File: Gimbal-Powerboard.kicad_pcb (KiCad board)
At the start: 2 copper layers, 165 parts, among them Q1 Q_PMOS_GDS, Q2 Q_PMOS_GDS, Q3 SI4116DY, Q4 SI4116DY, Q5 SI4116DY, Q6 SI4116DY, Q7 SI4116DY, Q8 SI4116DY, U1 DRV8301, U2 NUP4201MR6, U27 2P2T_Switch, U3 LAUNCHXL-F28069M_Launchpad_J1, U4 ACS711, U5 Molex_SL-3, U6 Molex_SL-5, U7 ACS711, U8 MAX_3232

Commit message: Created traces for MAX3232, part of DRV8301
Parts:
- added REF**: Via_P1.27mm_5x5, MRDT_Drill_Holes:Via_.6mm, F.Cu at (141.2, 96.6)
- C10, C11, C12, C13, C14, C15, C16, C17, C18, C20, C21, C23, C24, C25, C26, C27, C3, C32, C33, C34, C35, C4, C6, C7, C8, C9: footprint Capacitors_SMD:C_0805_HandSoldering -> Capacitors_SMD:C_0603_HandSoldering
- C36, C41, C42, C43: footprint Capacitors_SMD:C_0805_HandSoldering -> Capacitors_SMD:C_0603_HandSoldering; moved to B.Cu
- R1, R10, R11, R12, R13, R14, R15, R16, R17, R18, R19, R2, R20, R21, R22, R23, R24, R25, R26, R27, R28, R29, R3, R30, R31, R32, R33, R34, R35, R36, R37, R4, R5, R6, R7, R8, R9: footprint Resistors_SMD:R_0805_HandSoldering -> Capacitors_SMD:C_0603_HandSoldering
- U8: moved to B.Cu
- moved D16 350.5 mm to (317.6, 132.5)
- moved C32 349.8 mm to (357.3, 148.0)
- moved D12 348.0 mm to (318.6, 147.7)
- moved D14 345.1 mm to (335.4, 105.0)
- moved TP6 339.8 mm to (341.4, 138.4)
- moved R27 332.3 mm to (337.4, 144.3)
- moved D15 332.1 mm to (332.6, 75.6)
- moved R29 322.4 mm to (349.6, 151.0)
- moved TP9 314.7 mm to (346.1, 127.6)
- moved C7 313.4 mm to (342.3, 92.3)
- moved R33 310.1 mm to (347.9, 98.3)
- moved TP11 307.6 mm to (347.3, 84.6)
- moved TP3 304.3 mm to (332.6, 136.9)
- moved C11 301.7 mm to (348.7, 91.8)
- moved TP10 299.7 mm to (341.8, 41.4)
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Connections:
- net PVDD renamed 12VACT
- net PVDDSENSE renamed 12VACTSENSE
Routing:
- net VCC: track 0.00 -> 110.1 mm, vias 0 -> 3
- net UART_RX: track 0.00 -> 82.9 mm, vias 0 -> 2
- net UART_TX: track 0.00 -> 79.9 mm, vias 0 -> 2
- net PWM_IN: track 0.00 -> 67.1 mm
- net INL_C/PWM_IN_1: track 0.00 -> 57.5 mm, vias 0 -> 4
- net INL_C/PWM_IN_2: track 0.00 -> 53.2 mm, vias 0 -> 2
- net INL_C: track 0.00 -> 41.3 mm, vias 0 -> 1
- net NSCS: track 0.00 -> 34.0 mm, vias 0 -> 1
- net INH_A: track 0.00 -> 33.9 mm, vias 0 -> 1
- net SCLK: track 0.00 -> 33.3 mm, vias 0 -> 1
- net INL_A: track 0.00 -> 32.7 mm, vias 0 -> 1
- net INH_B: track 0.00 -> 31.4 mm, vias 0 -> 1
- net SDO: track 0.00 -> 31.4 mm, vias 0 -> 1
- net INL_B: track 0.00 -> 30.1 mm, vias 0 -> 1
- net SDI: track 0.00 -> 29.4 mm, vias 0 -> 1
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- added copper zone on B.Cu, net 12VACT
- added copper zone on F.Cu, net PVDD

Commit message: Finished component placement for DRV8301, phase C
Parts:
- C35: moved to B.Cu
- moved C32 250.8 mm to (116.2, 78.6)
- moved C11 248.8 mm to (101.3, 65.4)
- moved D11 248.8 mm to (76.3, 55.9)
- moved D15 248.8 mm to (85.2, 49.1)
- moved D8 248.8 mm to (96.8, 82.0)
- moved R22 248.8 mm to (80.1, 75.3)
- moved R33 248.8 mm to (100.5, 71.9)
- moved R36 248.8 mm to (91.4, 59.2)
- moved TP11 248.8 mm to (99.9, 58.2)
- moved TP5 248.8 mm to (78.5, 65.2)
- moved TP8 248.8 mm to (92.3, 51.8)
- moved C34 248.8 mm to (107.1, 60.7)
- moved C7 248.8 mm to (94.9, 65.9)
- moved D14 248.8 mm to (88.0, 78.6)
- moved R13 248.8 mm to (85.1, 61.1)
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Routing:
- net INL_C/PWM_IN_1: track 57.5 -> 0.00 mm, vias 4 -> 0
- net INL_C/PWM_IN_2: track 53.2 -> 0.79 mm, vias 2 -> 0
- net VCC: track 110.1 -> 63.9 mm, vias 3 -> 1
- net INL_C: track 41.3 -> 0.00 mm, vias 1 -> 0
- net PWM_IN: track 67.1 -> 31.0 mm
- net Net-(D16-Pad2): track 0.00 -> 24.6 mm, vias 0 -> 1
- net NSCS: track 34.0 -> 9.39 mm, vias 1 -> 0
- net DC_CAL: track 16.3 -> 38.6 mm, vias 0 -> 1
- net GND: track 9.56 -> 26.9 mm, vias 0 -> 1
- net Net-(R17-Pad1): track 11.3 -> 12.5 mm

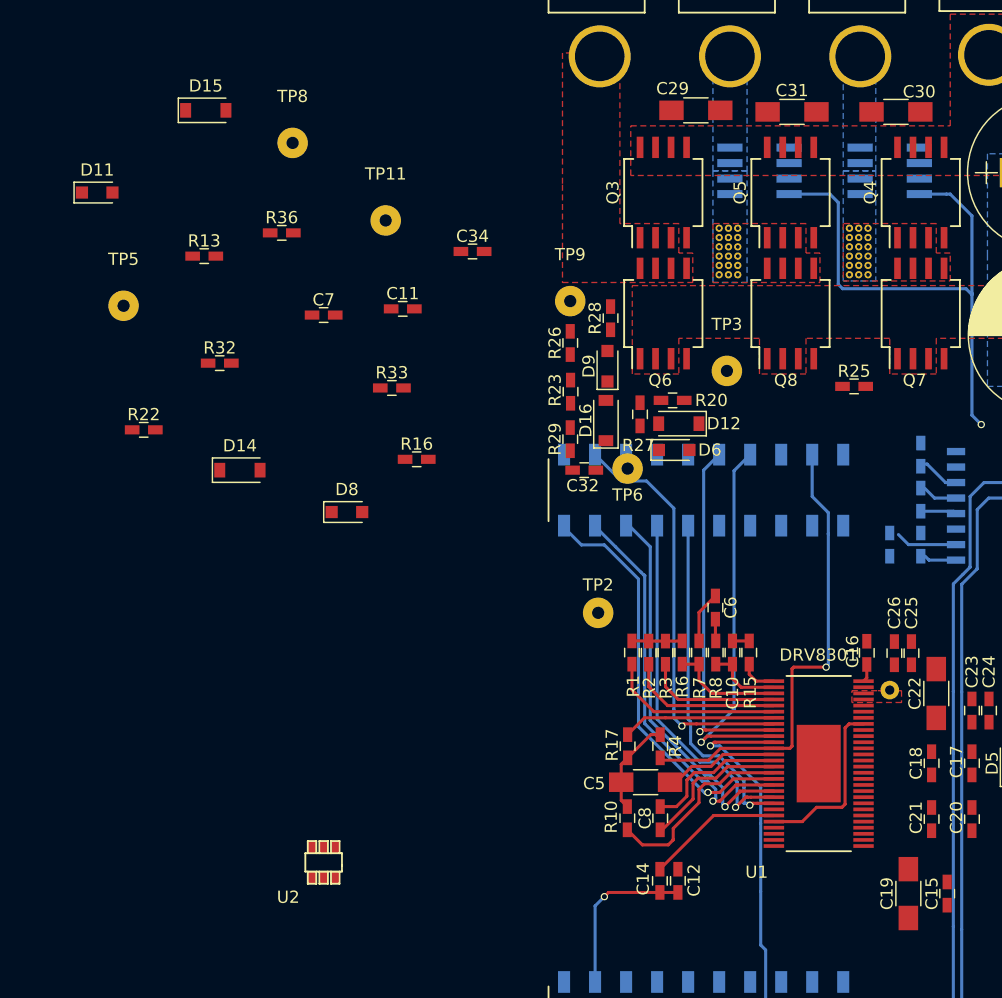
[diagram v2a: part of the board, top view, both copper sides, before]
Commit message: Added components for phase B circuitry
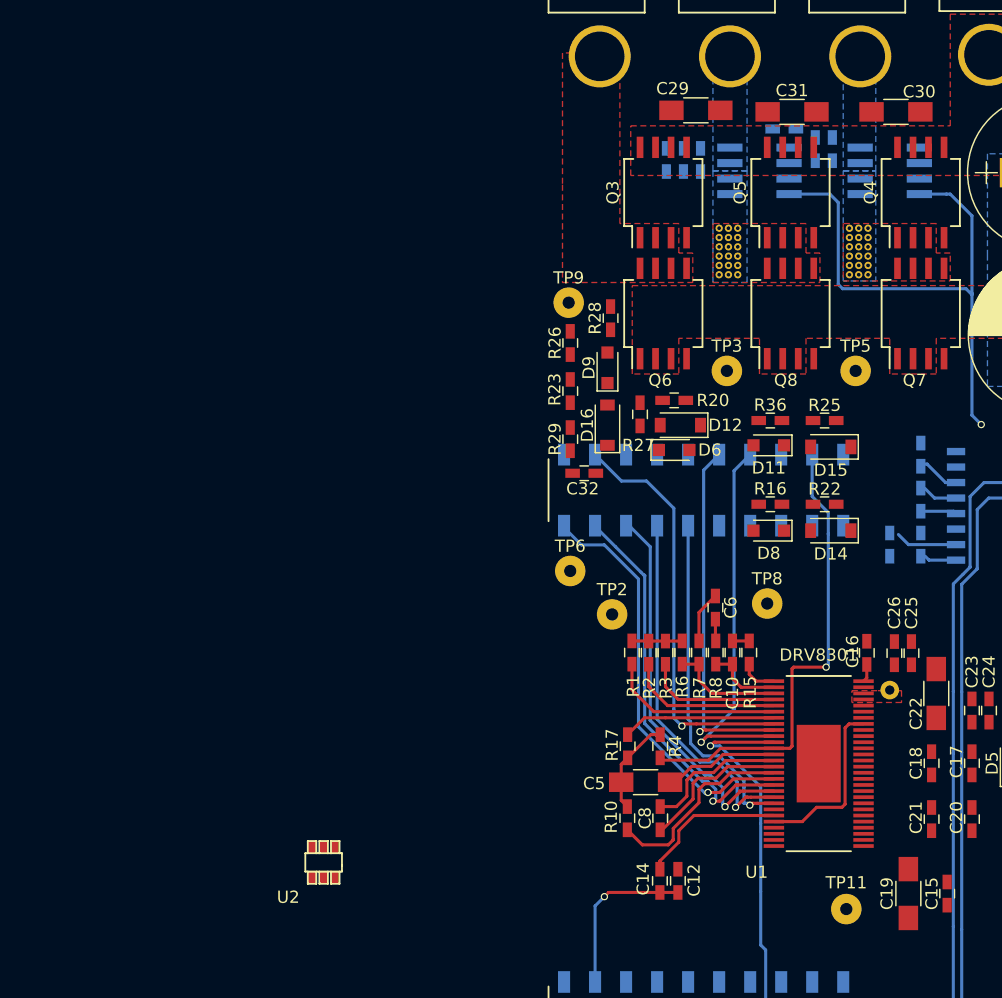
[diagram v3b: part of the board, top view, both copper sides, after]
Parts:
- C11, C34, C7, R13, R32, R33: moved to B.Cu
- moved TP11 67.8 mm to (137.7, 114.6)
- moved TP5 60.2 mm to (138.4, 70.5)
- moved D11 58.8 mm to (131.3, 76.6), turned to 180 degrees
- moved D15 58.1 mm to (136.4, 76.7), turned to 180 degrees
- moved R22 56.1 mm to (135.9, 81.4)
- moved TP8 54.2 mm to (131.2, 89.5)
- moved R13 50.8 mm to (135.1, 52.3), turned to 270 degrees
- moved D14 48.6 mm to (136.4, 83.6), turned to 180 degrees
- moved C7 43.8 mm to (136.5, 52.3), turned to 270 degrees
- moved R36 42.9 mm to (131.4, 74.5), turned to 180 degrees
- moved R32 42.7 mm to (125.7, 53.2), turned to 90 degrees
- moved D8 34.6 mm to (131.3, 83.6), turned to 180 degrees
- moved C11 34.5 mm to (132.6, 50.7)
- moved R33 30.3 mm to (124.3, 53.2), turned to 270 degrees
- moved R16 29.2 mm to (131.4, 81.4), turned to 180 degrees
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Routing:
- net Net-(D16-Pad2): track 24.6 -> 0.00 mm, vias 1 -> 0
- net NSCS: track 9.39 -> 34.0 mm, vias 0 -> 1
- net Net-(C14-Pad1): track 11.2 -> 12.1 mm

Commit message: Finished component placement, beginning the last of traces and silkscreen work
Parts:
- C27, C33, C9, R30, R31, R37: moved to B.Cu
- moved C9 200.5 mm to (147.1, 53.8), turned to 270 degrees
- moved D10 196.5 mm to (149.2, 78.4), turned to 180 degrees
- moved TP7 192.2 mm to (145.8, 73.0)
- moved TP4 192.0 mm to (154.9, 88.1)
- moved D17 191.4 mm to (144.3, 78.5)
- moved R21 191.0 mm to (143.6, 83.1), turned to 180 degrees
- moved TP10 189.7 mm to (155.2, 75.8)
- moved R30 188.0 mm to (143.0, 57.7), turned to 180 degrees
- moved R24 187.3 mm to (143.8, 76.5), turned to 180 degrees
- moved C33 181.5 mm to (143.0, 60.5), turned to 180 degrees
- moved R34 178.0 mm to (149.1, 82.9)
- moved R35 177.3 mm to (149.0, 76.5), turned to 180 degrees
- moved D13 174.8 mm to (144.1, 85.1)
- moved R37 172.7 mm to (145.7, 53.8), turned to 270 degrees
- moved R31 172.6 mm to (143.0, 59.1)
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
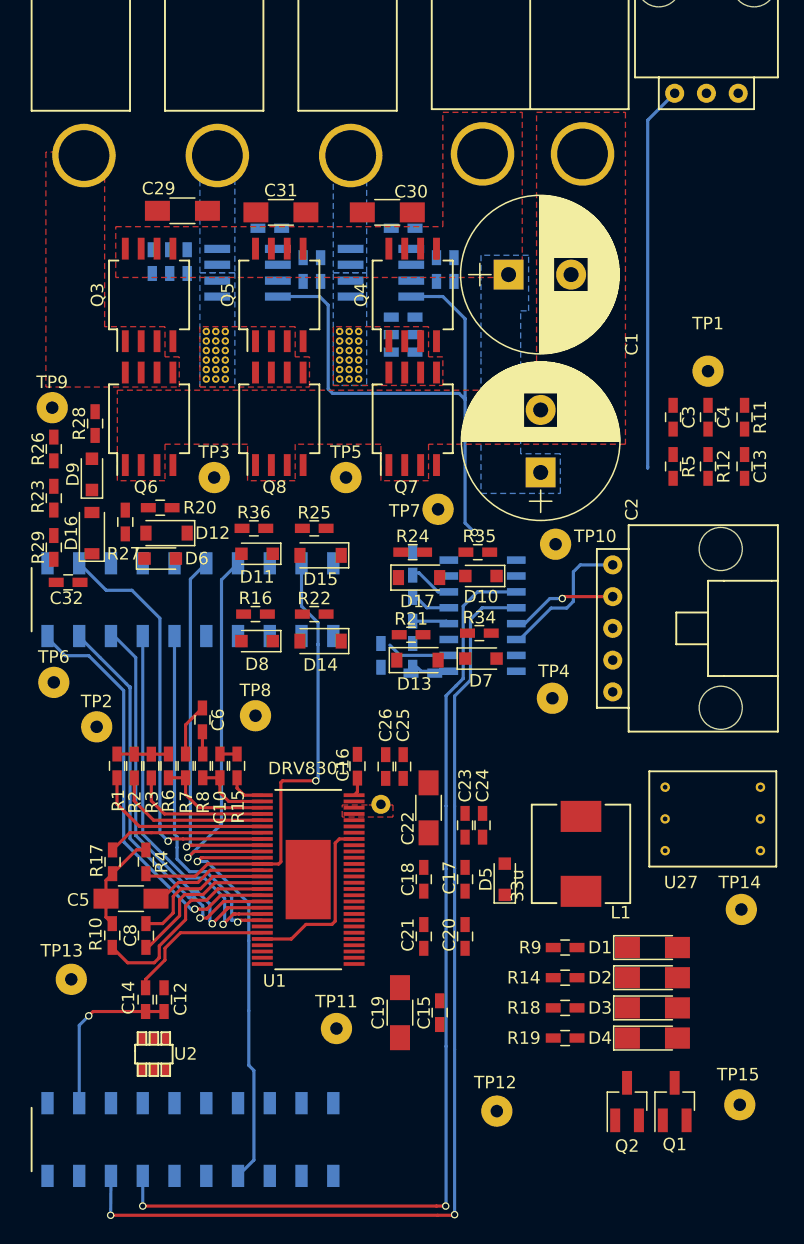
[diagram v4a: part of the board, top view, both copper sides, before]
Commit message: Finished routing for DRV8301
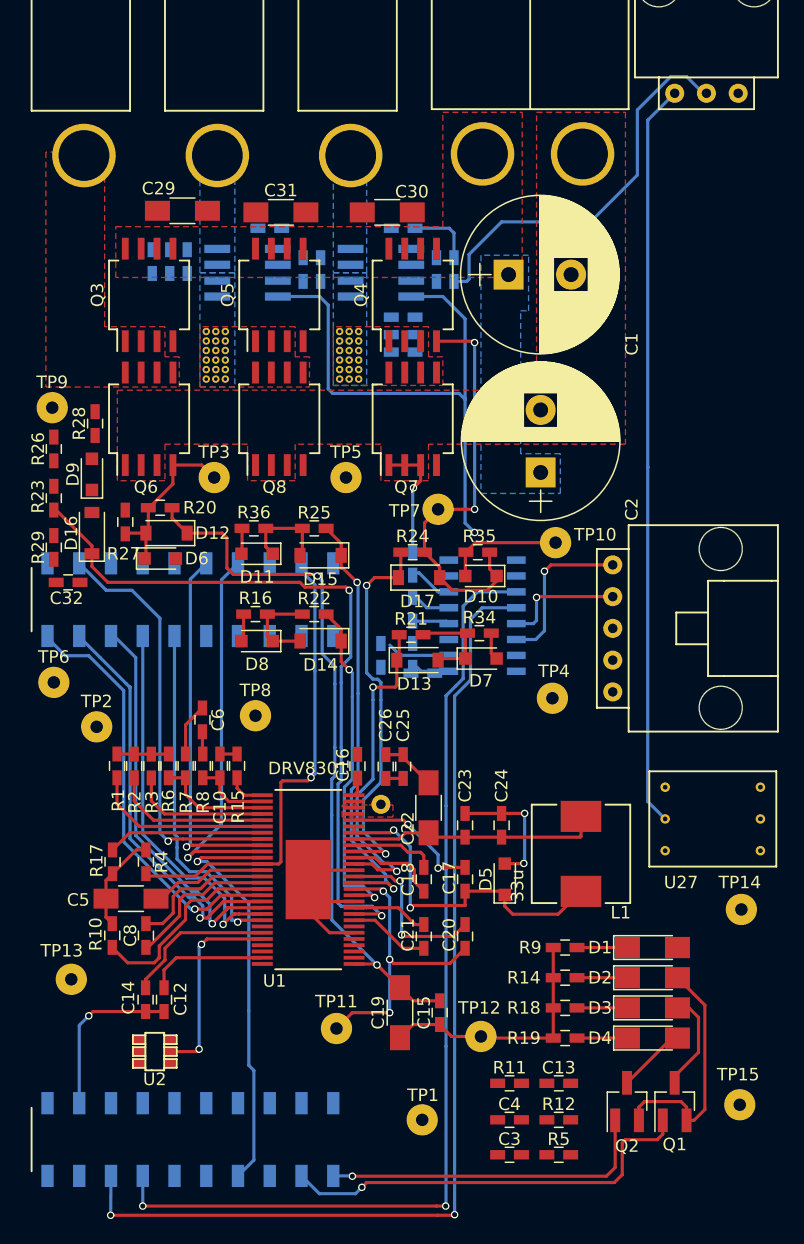
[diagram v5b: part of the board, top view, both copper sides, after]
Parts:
- moved TP1 64.1 mm to (144.5, 121.9)
- moved C3 60.4 mm to (151.5, 124.7), turned to 0 degrees
- moved C4 58.4 mm to (151.5, 121.9), turned to 0 degrees
- moved R11 56.5 mm to (151.5, 118.9), turned to 0 degrees
- moved R5 55.8 mm to (155.4, 124.7), turned to 0 degrees
- moved R12 53.6 mm to (155.4, 121.9), turned to 0 degrees
- moved C13 51.5 mm to (155.4, 118.9), turned to 0 degrees
- moved TP12 6.10 mm to (149.2, 115.2)
- moved C24 1.52 mm to (150.9, 98.3)
- moved U2 1.26 mm to (123.9, 116.4), turned to 270 degrees
- moved TP10 0.13 mm to (155.2, 75.7)
- turned C30 to 0 degrees
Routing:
- net VCC: track 63.9 -> 137.4 mm, vias 1 -> 3
- net GND: track 26.9 -> 96.8 mm, vias 1 -> 4
- net GH_C: track 0.00 -> 58.9 mm, vias 0 -> 2
- net GL_C: track 0.00 -> 57.3 mm, vias 0 -> 2
- net GH_B: track 0.00 -> 34.9 mm, vias 0 -> 2
- net NFAULT: track 14.5 -> 48.5 mm, vias 0 -> 1
- net Net-(D10-Pad1): track 0.00 -> 33.6 mm, vias 0 -> 2
- net GH_A: track 0.00 -> 31.0 mm, vias 0 -> 2
- net PWM_IN: track 31.0 -> 59.8 mm
- net Net-(C17-Pad2): track 0.00 -> 27.5 mm, vias 0 -> 2
- net GL_B: track 0.00 -> 27.4 mm, vias 0 -> 2
- net NOCTW: track 12.7 -> 39.3 mm, vias 0 -> 1
- net GL_A: track 0.00 -> 26.6 mm, vias 0 -> 2
- net SH_B: track 0.00 -> 25.8 mm, vias 0 -> 3
- net SH_A: track 0.00 -> 16.7 mm
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
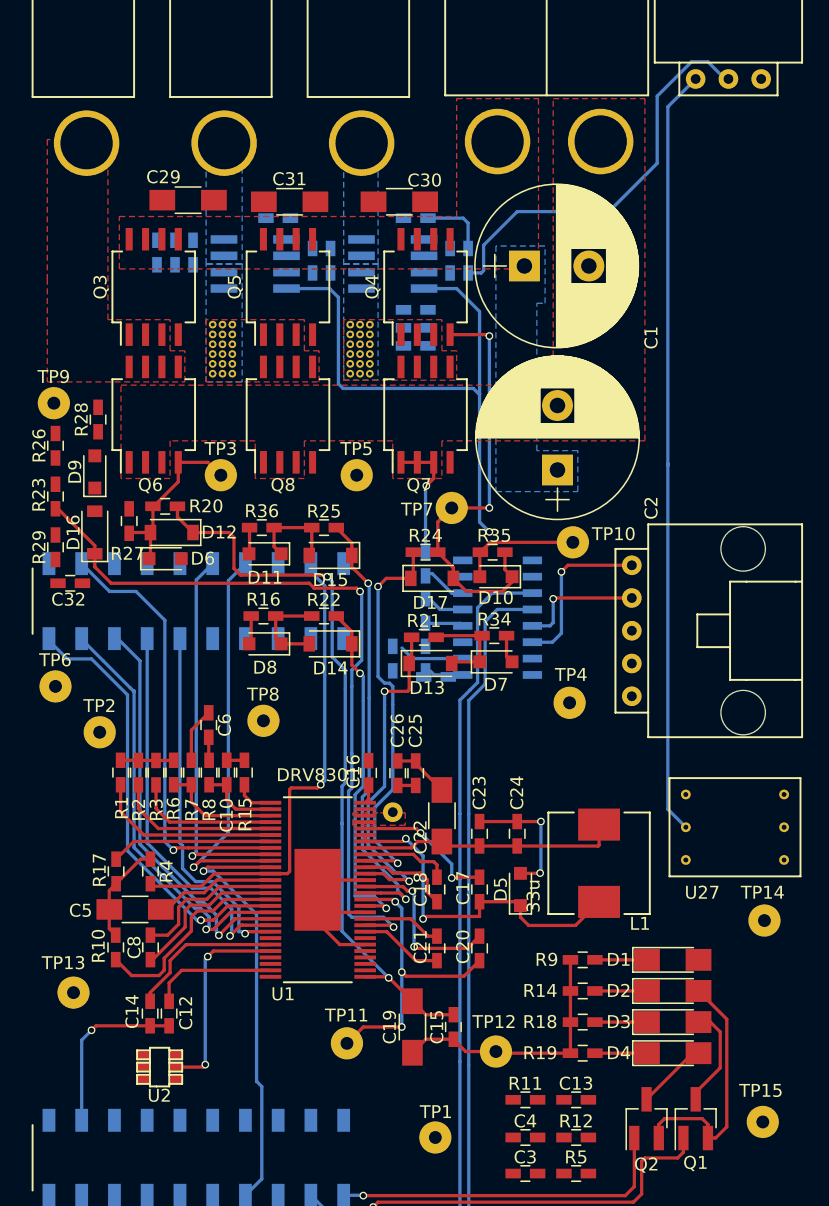
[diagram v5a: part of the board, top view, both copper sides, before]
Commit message: More routing progress, most of the top third of the board is completed
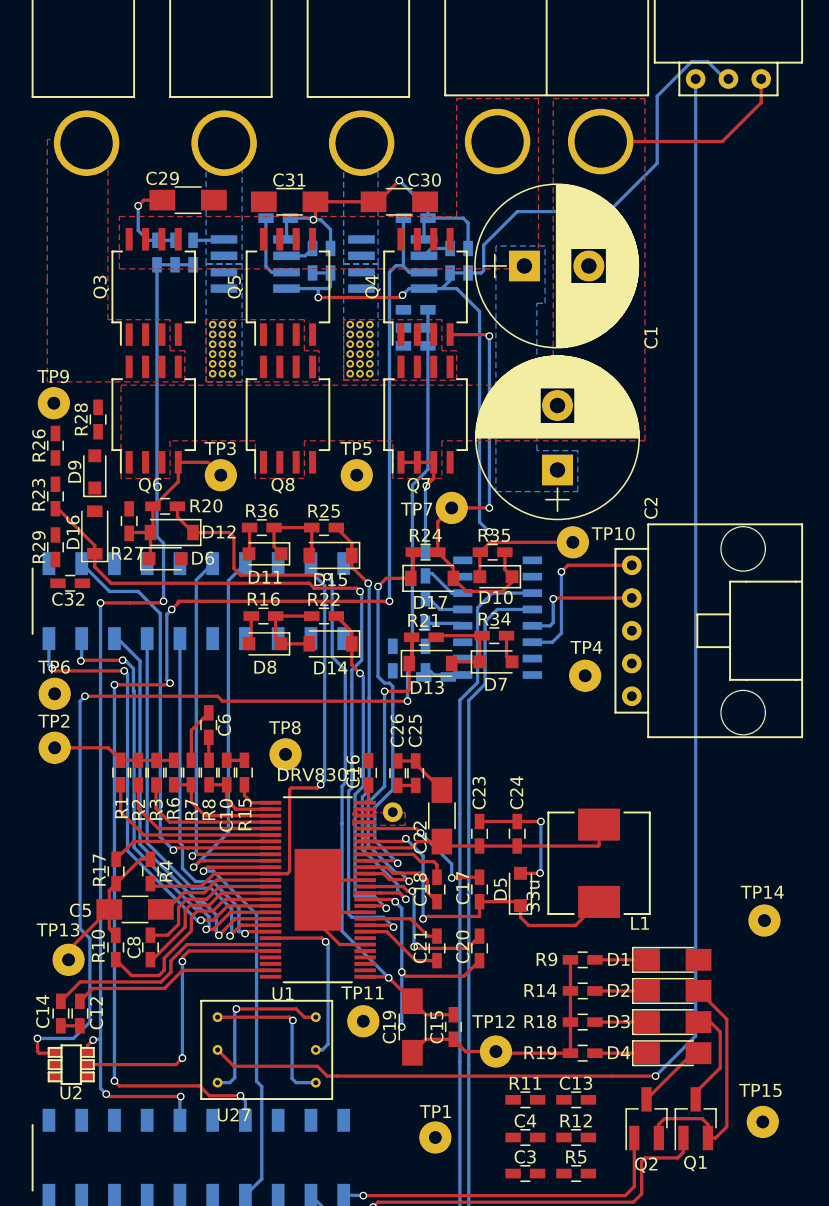
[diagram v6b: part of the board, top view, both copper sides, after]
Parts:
- moved U27 40.2 mm to (127.6, 117.6)
- moved C14 6.92 mm to (115.5, 112.2)
- moved C12 6.92 mm to (117.0, 112.2)
- moved U2 6.86 mm to (117.0, 116.2)
- moved TP2 3.70 mm to (115.0, 91.6)
- moved TP8 3.12 mm to (132.9, 92.1)
- moved TP13 2.57 mm to (116.1, 108.1)
- moved TP4 2.42 mm to (156.1, 86.0)
- moved TP11 2.13 mm to (138.9, 112.8)
- moved TP6 0.58 mm to (115.0, 87.4)
- turned C29 to 180 degrees
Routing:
- net CURRENTSENSEA: track 0.00 -> 103.0 mm, vias 0 -> 6
- net ASENSE: track 0.00 -> 89.0 mm, vias 0 -> 3
- net BSENSE: track 0.00 -> 81.8 mm, vias 0 -> 5
- net PWM_IN: track 59.8 -> 113.4 mm, vias 0 -> 1
- net GND: track 96.8 -> 133.7 mm, vias 4 -> 6
- net INL_C: track 0.00 -> 13.6 mm, vias 0 -> 1
- net INL_C/PWM_IN_1: track 0.00 -> 13.4 mm, vias 0 -> 1
- net INL_C/PWM_IN_2: track 0.79 -> 13.2 mm, vias 0 -> 1
- net VCC: track 137.4 -> 145.4 mm, vias 3 -> 5
- net Net-(C14-Pad1): track 12.1 -> 18.6 mm
- net Net-(C12-Pad2): track 9.69 -> 15.8 mm
- net CURRENTSENSEB: track 0.00 -> 5.53 mm
- net Net-(C42-Pad2): track 5.06 -> 0.00 mm
- net SH_B: track 25.8 -> 21.1 mm
- net MTB: track 0.00 -> 2.43 mm
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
